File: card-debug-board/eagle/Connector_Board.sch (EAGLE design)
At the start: 39 parts, among them J1 ORESAT-DEBUG-CONNECTOR-CARD, J3 USB_A_SMT_FEMALE, Q1 MOSFET-PCH-SOT23-6, SW1 B3F-1000, U1 FT230XS-R

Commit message: Re-Done with mirrored edge connector
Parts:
- J1: value ORESAT-DEBUG-CONNECTOR-CARD -> ORESAT-DEBUG-CONNECTOR-MIRRORED-CARD; device oresat-edge_connector:ORESAT-DEBUG-CONNECTOR-CARD -> oresat-debug-connector:ORESAT-DEBUG-CONNECTOR-MIRRORED-CARD
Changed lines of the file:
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@@
 <part name="GND8" library="supply1" library_urn="urn:adsk.eagle:library:371" deviceset="GND" device=""/>
 <part name="GND9" library="supply1" library_urn="urn:adsk.eagle:library:371" deviceset="GND" device=""/>
-<part name="J1" library="oresat-edge_connector" deviceset="ORESAT-DEBUG-CONNECTOR" device="-CARD">
+<part name="J1" library="oresat-debug-connector" deviceset="ORESAT-DEBUG-CONNECTOR-MIRRORED" device="-CARD">
 <attribute name="DESCRIPTION" value="20 Position FPC Connector Contacts, Bottom 0.020&quot; (0.50mm) Surface Mount, Right Angle"/>
 <attribute name="DIGI-KEY_PART_NUMBER" value="A100287CT-ND"/>

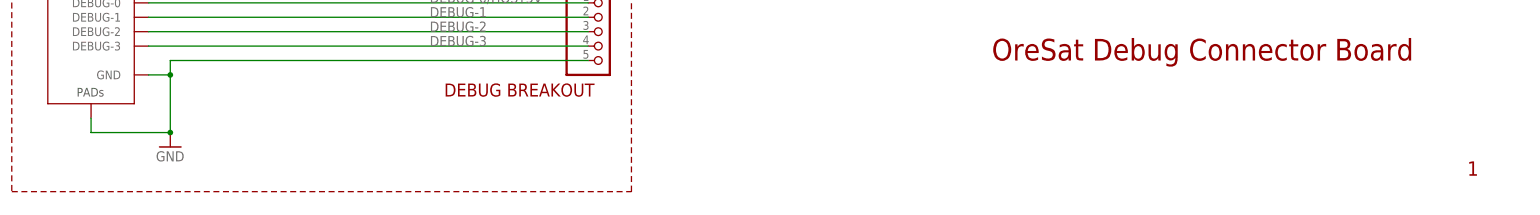
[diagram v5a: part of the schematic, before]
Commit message: Clean up text , added gnd via's
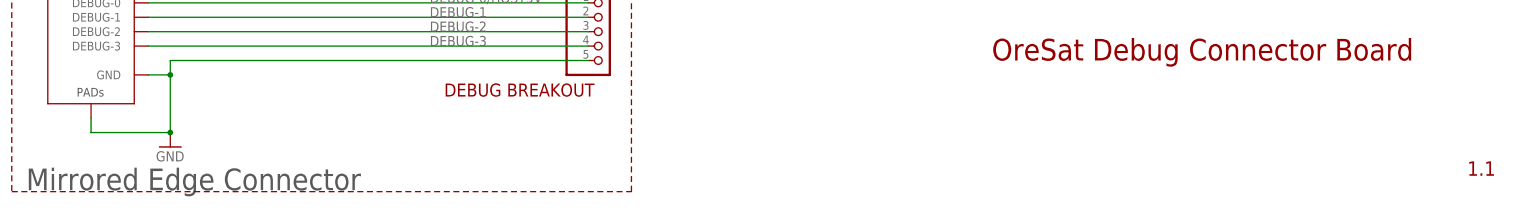
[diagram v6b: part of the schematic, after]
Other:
- note added: "1.1"
- note added: "Mirrored Edge Connector"
- note removed: "1"
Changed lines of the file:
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@@
 <attribute name="MANUFACTURER_PART_NUMBER" value="629105136821"/>
 </part>
-<part name="J3" library="SparkFun-Connectors" library_urn="urn:adsk.eagle:library:513" deviceset="USB_A" device="_SMT_FEMALE" package3d_urn="urn:adsk.eagle:package:38297/1">
+<part name="J3" library="SparkFun-Connectors" library_urn="urn:adsk.eagle:library:513" deviceset="USB_A" device="_SMT_FEMALE" package3d_urn="urn:adsk.eagle:package:38297/1" value="USB_A_SMT_FEMALE">
 <attribute name="DESCRIPTION" value="SparkFun Accessories USB Female Type A SMD Connector"/>
 <attribute name="MANUFACTURER" value="SparkFun"/>
@@
 <wire x1="7.62" y1="4.826" x2="116.84" y2="4.826" width="0.1524" layer="94" style="shortdash"/>
 <text x="180.34" y="27.94" size="3.81" layer="94">OreSat Debug Connector Board</text>
-<text x="264.16" y="7.62" size="2.54" layer="94">1</text>
+<text x="264.16" y="7.62" size="2.54" layer="94">1.1</text>
 <text x="53.34" y="88.9" size="2.286" layer="94">Power
 Select</text>
@@
 <text x="26.67" y="168.91" size="1.778" layer="97" rot="R90">TX</text>
 <text x="27.94" y="86.36" size="2.286" layer="94">VBUSP Supply</text>
+<text x="10.16" y="5.08" size="3.81" layer="97">Mirrored Edge Connector</text>
 </plain>
 <instances>

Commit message: Switched to thin mirrored edge connector
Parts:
- J1: value ORESAT-DEBUG-CONNECTOR-MIRRORED-CARD -> ORESAT-DEBUG-CONNECTOR-MIRRORED-SOLAR; device oresat-debug-connector:ORESAT-DEBUG-CONNECTOR-MIRRORED-CARD -> oresat-debug-connector:ORESAT-DEBUG-CONNECTOR-MIRRORED-SOLAR
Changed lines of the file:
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@@
 <part name="GND8" library="supply1" library_urn="urn:adsk.eagle:library:371" deviceset="GND" device=""/>
 <part name="GND9" library="supply1" library_urn="urn:adsk.eagle:library:371" deviceset="GND" device=""/>
-<part name="J1" library="oresat-debug-connector" deviceset="ORESAT-DEBUG-CONNECTOR-MIRRORED" device="-CARD">
+<part name="J1" library="oresat-debug-connector" deviceset="ORESAT-DEBUG-CONNECTOR-MIRRORED" device="-SOLAR" value="ORESAT-DEBUG-CONNECTOR-MIRRORED-SOLAR">
 <attribute name="DESCRIPTION" value="20 Position FPC Connector Contacts, Bottom 0.020&quot; (0.50mm) Surface Mount, Right Angle"/>
 <attribute name="DIGI-KEY_PART_NUMBER" value="A100287CT-ND"/>

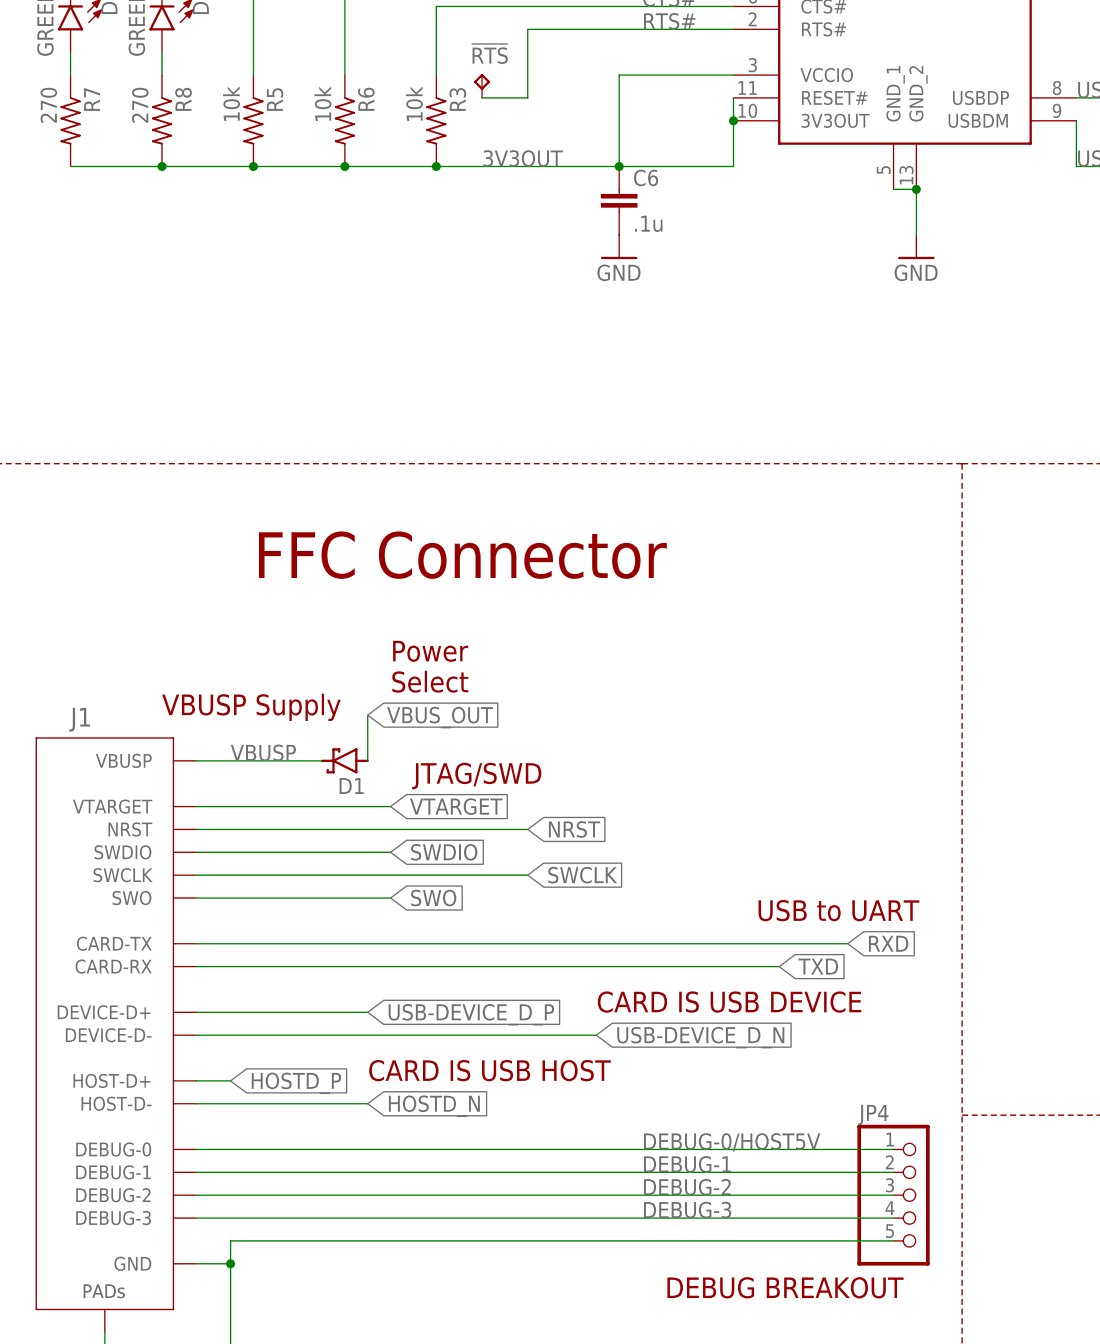
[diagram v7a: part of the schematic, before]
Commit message: Added jumper and diode for 3.0V supply for solar for debugging without solar power.
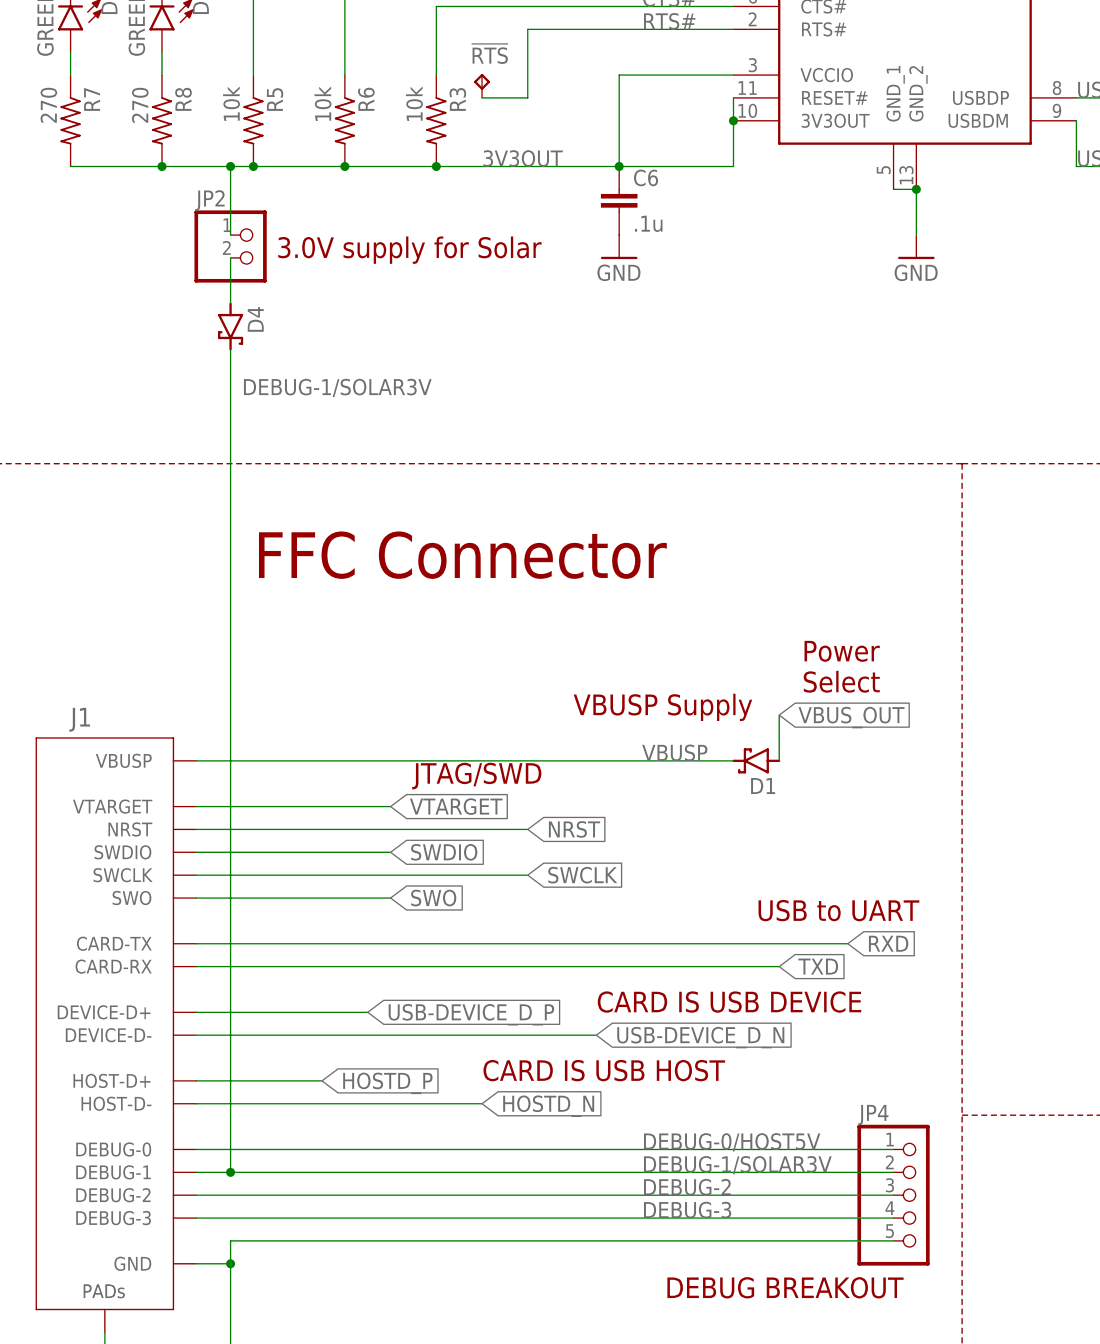
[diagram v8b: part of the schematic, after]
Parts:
- added D4: CDBU0520, D-Comchip_Schottky_Diode_CDBU0520:CDBU0520
- added JP2: (no value), pinhead:PINHD-1X2
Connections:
- removed net DEBUG-1: J1.DEBUG-1, JP4.2
- new net DEBUG-1/SOLAR3V: D4.C, J1.DEBUG-1, JP4.2
- new net N$7: D4.A, JP2.2
- net 3V3OUT: now also JP2.1
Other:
- note added: "3.0V supply for Solar"
- moved on the sheet: D1
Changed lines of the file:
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@@
 <?xml version="1.0" encoding="utf-8"?>
 <!DOCTYPE eagle SYSTEM "eagle.dtd">
-<eagle version="9.5.2">
+<eagle version="9.6.1">
 <drawing>
 <settings>
@@
 <setting verticaltext="up"/>
 </settings>
-<grid distance="0.1" unitdist="inch" unit="inch" style="lines" multiple="1" display="no" altdistance="0.01" altunitdist="inch" altunit="inch"/>
+<grid distance="0.05" unitdist="inch" unit="inch" style="lines" multiple="2" display="no" altdistance="0.01" altunitdist="inch" altunit="inch"/>
 <layers>
 <layer number="1" name="Top" color="4" fill="1" visible="no" active="no"/>
@@
 </part>
 <part name="GND15" library="supply1" library_urn="urn:adsk.eagle:library:371" deviceset="GND" device=""/>
+<part name="D4" library="D-Comchip_Schottky_Diode_CDBU0520" deviceset="CDBU0520" device="">
+<attribute name="DESCRIPTION" value="Diode Schottky 20V 500mA Surface Mount 0603/SOD-523F"/>
+<attribute name="DIGI-KEY_PART_NUMBER" value="641-1332-1-ND"/>
+<attribute name="MANUFACTURER" value="Comchip Technology"/>
+<attribute name="MANUFACTURER_PART_NUMBER" value="CDBU0520"/>
+</part>
+<part name="JP2" library="pinhead" library_urn="urn:adsk.eagle:library:325" deviceset="PINHD-1X2" device="" package3d_urn="urn:adsk.eagle:package:22435/2">
+<attribute name="DESCRIPTION" value="Connector Header Through Hole 2 position 0.100&quot; (2.54mm)"/>
+<attribute name="DIGI-KEY_PART_NUMBER" value="732-5315-ND"/>
+<attribute name="MANUFACTURER" value="Würth Elektronik"/>
+<attribute name="MANUFACTURER_PART_NUMBER" value="61300211121"/>
+</part>
 </parts>
 <sheets>
@@
 <text x="180.34" y="27.94" size="3.81" layer="94">OreSat Debug Connector Board</text>
 <text x="264.16" y="7.62" size="2.54" layer="94">1.1</text>
-<text x="53.34" y="88.9" size="2.286" layer="94">Power
+<text x="99.06" y="88.9" size="2.286" layer="94">Power
 Select</text>
 <text x="55.88" y="78.74" size="2.286" layer="94">JTAG/SWD</text>
 <text x="93.98" y="63.5" size="2.286" layer="94">USB to UART</text>
 <text x="76.2" y="53.34" size="2.286" layer="94">CARD IS USB DEVICE</text>
-<text x="50.8" y="45.72" size="2.286" layer="94">CARD IS USB HOST</text>
+<text x="63.5" y="45.72" size="2.286" layer="94">CARD IS USB HOST</text>
 <text x="83.82" y="21.59" size="2.286" layer="94">DEBUG BREAKOUT</text>
 <text x="16.51" y="168.91" size="1.778" layer="97" rot="R90">RX</text>
 <text x="26.67" y="168.91" size="1.778" layer="97" rot="R90">TX</text>
-<text x="27.94" y="86.36" size="2.286" layer="94">VBUSP Supply</text>
+<text x="73.66" y="86.36" size="2.286" layer="94">VBUSP Supply</text>
 <text x="10.16" y="5.08" size="3.81" layer="97">Mirrored Edge Connector</text>
+<text x="40.64" y="137.16" size="2.286" layer="94">3.0V supply for Solar</text>
 </plain>
 <instances>
@@
 <attribute name="VALUE" x="238.76" y="50.8" size="1.778" layer="96"/>
 </instance>
-<instance part="D1" gate="G$1" x="48.26" y="81.28" smashed="yes" rot="R180">
-<attribute name="NAME" x="50.546" y="79.375" size="1.778" layer="95" rot="R180"/>
-<attribute name="DIGI-KEY_PART_NUMBER" x="48.26" y="81.28" size="1.778" layer="96" rot="R180" display="off"/>
-<attribute name="MANUFACTURER_PART_NUMBER" x="48.26" y="81.28" size="1.778" layer="96" rot="R180" display="off"/>
-<attribute name="MANUFACTURER" x="48.26" y="81.28" size="1.778" layer="96" rot="R180" display="off"/>
-<attribute name="DESCRIPTION" x="48.26" y="81.28" size="1.778" layer="96" rot="R180" display="off"/>
+<instance part="D1" gate="G$1" x="93.98" y="81.28" smashed="yes" rot="R180">
+<attribute name="NAME" x="96.266" y="79.375" size="1.778" layer="95" rot="R180"/>
+<attribute name="DIGI-KEY_PART_NUMBER" x="93.98" y="81.28" size="1.778" layer="96" rot="R180" display="off"/>
+<attribute name="MANUFACTURER_PART_NUMBER" x="93.98" y="81.28" size="1.778" layer="96" rot="R180" display="off"/>
+<attribute name="MANUFACTURER" x="93.98" y="81.28" size="1.778" layer="96" rot="R180" display="off"/>
+<attribute name="DESCRIPTION" x="93.98" y="81.28" size="1.778" layer="96" rot="R180" display="off"/>
 </instance>
 <instance part="CM1" gate="A" x="160.02" y="78.74" smashed="yes">
@@
 <attribute name="VALUE" x="148.59" y="46.99" size="1.778" layer="96"/>
 </instance>
+<instance part="D4" gate="G$1" x="35.56" y="129.54" smashed="yes" rot="R270">
+<attribute name="NAME" x="37.465" y="131.826" size="1.778" layer="95" rot="R270"/>
+<attribute name="DIGI-KEY_PART_NUMBER" x="35.56" y="129.54" size="1.778" layer="96" rot="R270" display="off"/>
+<attribute name="MANUFACTURER_PART_NUMBER" x="35.56" y="129.54" size="1.778" layer="96" rot="R270" display="off"/>
+<attribute name="MANUFACTURER" x="35.56" y="129.54" size="1.778" layer="96" rot="R270" display="off"/>
+<attribute name="DESCRIPTION" x="35.56" y="129.54" size="1.778" layer="96" rot="R270" display="off"/>
+</instance>
+<instance part="JP2" gate="G$1" x="38.1" y="137.16" smashed="yes">
+<attribute name="NAME" x="31.75" y="142.875" size="1.778" layer="95"/>
+<attribute name="VALUE" x="31.75" y="132.08" size="1.778" layer="96"/>
+<attribute name="DIGI-KEY_PART_NUMBER" x="38.1" y="137.16" size="1.778" layer="96" display="off"/>
+<attribute name="MANUFACTURER" x="38.1" y="137.16" size="1.778" layer="96" display="off"/>
+<attribute name="MANUFACTURER_PART_NUMBER" x="38.1" y="137.16" size="1.778" layer="96" display="off"/>
+<attribute name="DESCRIPTION" x="38.1" y="137.16" size="1.778" layer="96" display="off"/>
+</instance>
 </instances>
 <busses>
@@
 <net name="HOSTD_P" class="1">
 <segment>
-<label x="35.56" y="45.72" size="1.778" layer="95" xref="yes"/>
+<label x="45.72" y="45.72" size="1.778" layer="95" xref="yes"/>
 <pinref part="J1" gate="G$1" pin="HOST-D+"/>
-<wire x1="31.75" y1="45.72" x2="35.56" y2="45.72" width="0.1524" layer="91"/>
+<wire x1="31.75" y1="45.72" x2="45.72" y2="45.72" width="0.1524" layer="91"/>
 </segment>
 <segment>
@@
 <net name="HOSTD_N" class="1">
 <segment>
-<label x="50.8" y="43.18" size="1.778" layer="95" xref="yes"/>
+<label x="63.5" y="43.18" size="1.778" layer="95" xref="yes"/>
 <pinref part="J1" gate="G$1" pin="HOST-D-"/>
-<wire x1="31.75" y1="43.18" x2="50.8" y2="43.18" width="0.1524" layer="91"/>
+<wire x1="31.75" y1="43.18" x2="63.5" y2="43.18" width="0.1524" layer="91"/>
 </segment>
 <segment>
@@
 <pinref part="R7" gate="R" pin="2"/>
 <wire x1="48.26" y1="147.32" x2="38.1" y2="147.32" width="0.1524" layer="91"/>
-<wire x1="38.1" y1="147.32" x2="27.94" y2="147.32" width="0.1524" layer="91"/>
+<wire x1="38.1" y1="147.32" x2="35.56" y2="147.32" width="0.1524" layer="91"/>
+<wire x1="35.56" y1="147.32" x2="27.94" y2="147.32" width="0.1524" layer="91"/>
 <wire x1="27.94" y1="147.32" x2="17.78" y2="147.32" width="0.1524" layer="91"/>
 <pinref part="R8" gate="R" pin="2"/>
@@
 <wire x1="91.44" y1="147.32" x2="78.74" y2="147.32" width="0.1524" layer="91"/>
 <wire x1="78.74" y1="157.48" x2="78.74" y2="147.32" width="0.1524" layer="91"/>
+<junction x="35.56" y="147.32"/>
+<wire x1="35.56" y1="139.7" x2="35.56" y2="147.32" width="0.1524" layer="91"/>
+<pinref part="JP2" gate="G$1" pin="1"/>
 </segment>
 </net>
@@
 <segment>
 <pinref part="D1" gate="G$1" pin="C"/>
-<label x="35.56" y="81.28" size="1.778" layer="95"/>
-<wire x1="45.72" y1="81.28" x2="31.75" y2="81.28" width="0.1524" layer="91"/>
+<label x="81.28" y="81.28" size="1.778" layer="95"/>
+<wire x1="91.44" y1="81.28" x2="31.75" y2="81.28" width="0.1524" layer="91"/>
 <pinref part="J1" gate="G$1" pin="VBUSP"/>
 </segment>
@@
 </segment>
 <segment>
-<wire x1="50.8" y1="86.36" x2="50.8" y2="81.28" width="0.1524" layer="91"/>
+<wire x1="96.52" y1="86.36" x2="96.52" y2="81.28" width="0.1524" layer="91"/>
 <pinref part="D1" gate="G$1" pin="A"/>
-<label x="50.8" y="86.36" size="1.778" layer="95" xref="yes"/>
+<label x="96.52" y="86.36" size="1.778" layer="95" xref="yes"/>
 </segment>
 </net>
@@
 </segment>
 </net>
-<net name="DEBUG-1" class="0">
+<net name="DEBUG-1/SOLAR3V" class="0">
 <segment>
 <pinref part="J1" gate="G$1" pin="DEBUG-1"/>
-<wire x1="31.75" y1="35.56" x2="109.22" y2="35.56" width="0.1524" layer="91"/>
+<wire x1="31.75" y1="35.56" x2="35.56" y2="35.56" width="0.1524" layer="91"/>
 <label x="81.28" y="35.56" size="1.778" layer="95"/>
 <pinref part="JP4" gate="A" pin="2"/>
+<pinref part="D4" gate="G$1" pin="C"/>
+<wire x1="35.56" y1="35.56" x2="109.22" y2="35.56" width="0.1524" layer="91"/>
+<wire x1="35.56" y1="127" x2="35.56" y2="35.56" width="0.1524" layer="91"/>
+<junction x="35.56" y="35.56"/>
+<label x="36.83" y="121.92" size="1.778" layer="95"/>
 </segment>
 </net>
@@
 </segment>
 </net>
+<net name="N$7" class="0">
+<segment>
+<pinref part="D4" gate="G$1" pin="A"/>
+<wire x1="35.56" y1="132.08" x2="35.56" y2="137.16" width="0.1524" layer="91"/>
+<pinref part="JP2" gate="G$1" pin="2"/>
+</segment>
+</net>
